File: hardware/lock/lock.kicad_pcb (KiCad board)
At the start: 2 copper layers, 64 x 23 mm, 50 parts, among them J2 I2C JST-PH RA, J3 SOLENOID 12V, J4 UPDI PROG, J5 SERVO S/V+/GND, J6 HALL DOOR, J7 HALL BOLT, J8 SERVO2 S/V+/GND, Q1 AO3400A, Q2 AO3400A, Q3 AO3401A, Q4 AO3400A, Q5 AO3400A, U1 ATtiny1616, U2 MT3608

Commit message: lock: PCB checkpoint — footprint placement progress
Co-Authored-By: Claude Opus 4.8 (1M context) <noreply@anthropic.com>
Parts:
- moved C6 4.05 mm to (133.9, 68.0), turned to -90 degrees
- moved C4 2.25 mm to (131.0, 68.0)
- moved Q3 0.24 mm to (129.2, 72.1)
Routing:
- net /DRV/VSERVO: track 26.3 -> 23.1 mm
- net Net-(U2-FB): track 16.8 -> 19.4 mm
- net SERVO_SIG: track 65.2 -> 63.0 mm
- net VCC: track 71.5 -> 70.0 mm, vias 12 -> 11
- net VSOL: track 37.4 -> 38.4 mm
- net GND: track 17.4 -> 18.4 mm, vias 58 -> 69
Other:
- board text added: "Ephemerkey LockBoost RevA"

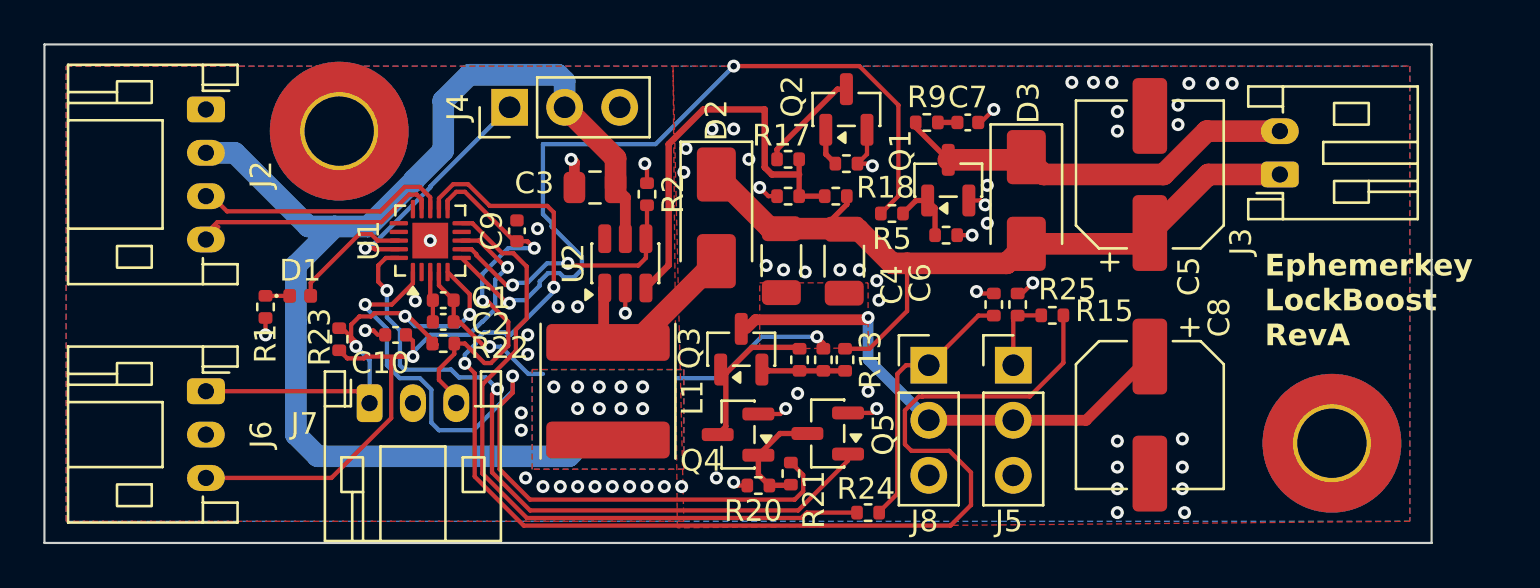
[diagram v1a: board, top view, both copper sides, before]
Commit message: lock: power from I2C connector (VSYS), LED on PC3; route board; ephemerkey J2=VSYS
Power move: the lock has NO local battery (J1 removed) — VCC and the boost/
actuator draw come from ephemerkey's VSYS rail over the I2C connector (J2.2).
- ephemerkey: J2.2 = VSYS (was +3V3); manifest note + DESIGN.md updated, regenerated.
- lock: README interface/architecture/BOM + servo source (R13=VSOL / R14=VSYS,
  no more VBAT) updated to match the as-wired board.
- Caveat documented: a 12V solenoid pull-in (~3-4A) exceeds a JST-PH contact and
  ephemerkey's load-share; favor the 6V servo / low-duty, or a dedicated feed.
- I2C pull-ups stay on ephemerkey at +3V3 (STM32 pins not >3.6V tolerant).

LED move: status LED (D1) is driven by PC3, not PA3 (PA3 now spare). Docs + manifest.

lock schematic + PCB are now hand-wired and fully routed (DRC: 0 unconnected,
0 schematic-parity). Manifest marked REFERENCE-OF-RECORD — do not regenerate
(would destroy the wiring). Verified with KiCad's own kicad-cli ERC/DRC.

Pending (owner fixing): PWR_FLAGs on VCC/GND, NC flags on unused pins, J6/J7 GND
thermal relief, minor stub/silk cleanups.

Co-Authored-By: Claude Opus 4.8 (1M context) <noreply@anthropic.com>
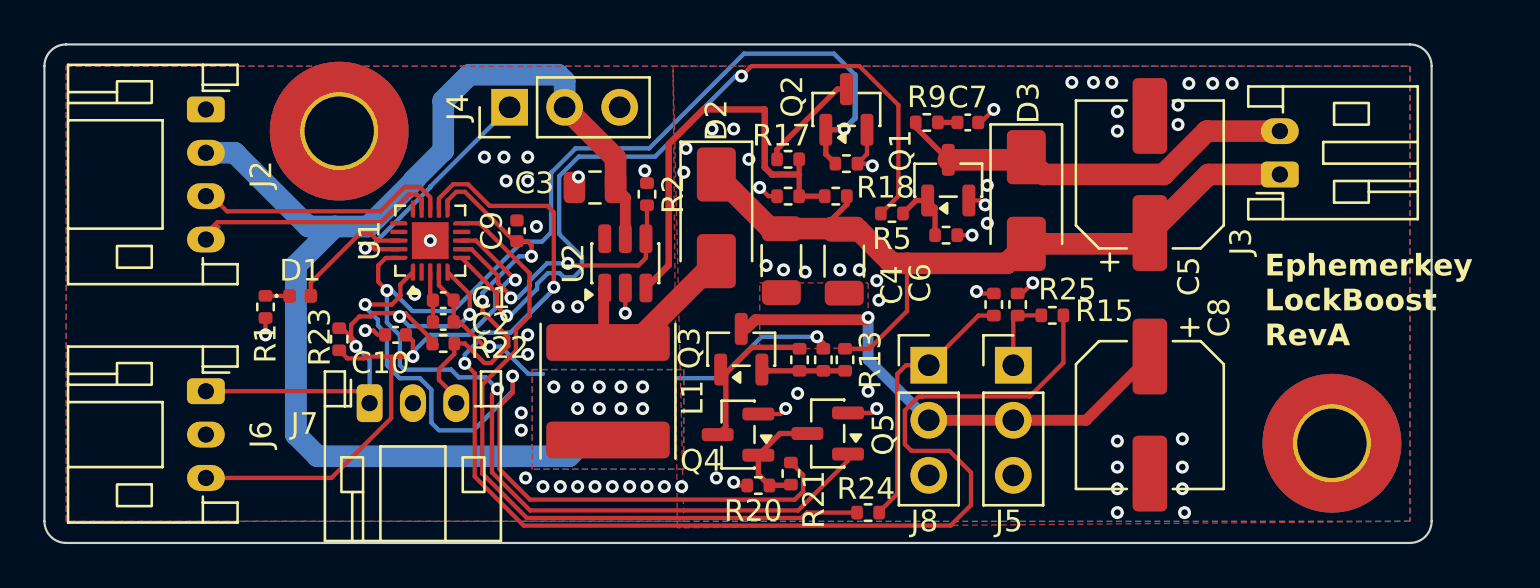
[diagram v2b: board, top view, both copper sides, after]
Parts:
- U1: footprint Package_DFN_QFN:QFN-20-1EP_3x3mm_P0.4mm_EP1.65x1.65mm -> Package_DFN_QFN:VQFN-20-1EP_3x3mm_P0.4mm_EP1.7x1.7mm
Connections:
- Q2 pad 1: BOOST_VEL -> BOOST_VSEL
- R18 pad 1: BOOST_VEL -> BOOST_VSEL
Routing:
- net BOOST_VSEL: track 33.6 -> 68.0 mm, vias 2 -> 3
- net BOOST_VEL: track 1.74 -> 0.00 mm
- net GND: track 18.4 -> 17.3 mm, vias 69 -> 74
- net SOL_PWM: track 37.8 -> 36.8 mm
- net SOL_BOOST_EN: track 12.3 -> 13.1 mm
- net /MCU/HALL_DOOR: track 27.6 -> 28.3 mm
- net /MCU/HALL_BOLT: track 19.3 -> 18.7 mm
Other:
- outline, holes or cut-outs redrawn

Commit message: lock: PCB edits — DRC/ERC cleanup in progress
Co-Authored-By: Claude Opus 4.8 (1M context) <noreply@anthropic.com>
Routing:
- net /MCU/HALL_DOOR: track 28.3 -> 27.8 mm
- net GND: vias 74 -> 75
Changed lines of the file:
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@@
+	)
+	(via
+		(at 130.75047 71.225)
+		(size 0.6)
+		(drill 0.3)
+		(layers "F.Cu" "B.Cu")
+		(free yes)
+		(net "GND")
 	)
 	(via
@@
 	)
 	(via
-		(at 131.1 68.4)
+		(at 131.2 68.2)
 		(size 0.6)
 		(drill 0.3)
@@
 	)
 	(via
-		(at 132.1 68.5)
+		(at 132.4 68.2)
 		(size 0.6)
 		(drill 0.3)
@@
 	)
 	(segment
-		(start 118.366486 68.507526)
-		(end 118.729265 68.870305)
-		(width 0.2)
-		(layer "F.Cu")
-		(net "/MCU/HALL_DOOR")
-	)
-	(segment
 		(start 110.97471 72.48471)
 		(end 111.741798 72.48471)
@@
 		(layer "B.Cu")
 		(net "/MCU/HALL_DOOR")
+	)
+	(segment
+		(start 129.3875 71.1125)
+		(end 130.05 70.45)
+		(width 0.5)
+		(layer "F.Cu")
+		(net "/DRV/VSERVO")
 	)
 	(segment
@@
 	)
 	(segment
+		(start 130.05 70.45)
+		(end 133.181371 70.45)
+		(width 0.5)
+		(layer "F.Cu")
+		(net "/DRV/VSERVO")
+	)
+	(segment
+		(start 133.181371 70.45)
+		(end 133.431371 70.7)
+		(width 0.5)
+		(layer "F.Cu")
+		(net "/DRV/VSERVO")
+	)
+	(segment
+		(start 145.06 75.34)
+		(end 141.7 75.34)
+		(width 0.5)
+		(layer "F.Cu")
+		(net "/DRV/VSERVO")
+	)
+	(segment
+		(start 141.7 75.34)
+		(end 137.8 75.34)
+		(width 0.5)
+		(layer "F.Cu")
+		(net "/DRV/VSERVO")
+	)
+	(segment
+		(start 133.431371 70.7)
+		(end 134.9 70.7)
+		(width 0.5)
+		(layer "F.Cu")
+		(net "/DRV/VSERVO")
+	)
+	(segment
 		(start 134.9 70.7)
 		(end 135 70.6)
@@
 		(net "/DRV/VSERVO")
 	)
-	(segment
-		(start 145.06 75.34)
-		(end 141.7 75.34)
-		(width 0.5)
-		(layer "F.Cu")
-		(net "/DRV/VSERVO")
-	)
-	(segment
-		(start 129.8 70.7)
-		(end 134.9 70.7)
-		(width 0.5)
-		(layer "F.Cu")
-		(net "/DRV/VSERVO")
-	)
-	(segment
-		(start 141.7 75.34)
-		(end 137.8 75.34)
-		(width 0.5)
-		(layer "F.Cu")
-		(net "/DRV/VSERVO")
-	)
-	(segment
-		(start 129.3875 71.1125)
-		(end 129.8 70.7)
-		(width 0.5)
-		(layer "F.Cu")
-		(net "/DRV/VSERVO")
-	)
 	(via
 		(at 135 70.6)
@@
 		(start 136.8 70.3)
 		(end 136.8 68.1)
-		(width 0.2)
+		(width 0.4)
 		(layer "F.Cu")
 		(net "VSOL")
@@
 		(start 135.06 72.04)
 		(end 136.8 70.3)
-		(width 0.2)
+		(width 0.4)
 		(layer "F.Cu")
 		(net "VSOL")
@@
 		(start 133.9375 72.04)
 		(end 135.06 72.04)
-		(width 0.2)
+		(width 0.4)
 		(layer "F.Cu")
 		(net "VSOL")
@@
 	)
 	(segment
-		(start 132.9375 71.770001)
-		(end 132.65534 71.487841)
-		(width 0.2)
+		(start 132.9375 72.04)
+		(end 132.9375 71.3375)
+		(width 0.4)
 		(layer "F.Cu")
 		(net "VCC")
@@
 		(start 115.2 69.12)
 		(end 115.88 69.8)
-		(width 0.2)
-		(layer "F.Cu")
-		(net "VCC")
-	)
-	(segment
-		(start 132.65534 71.487841)
-		(end 132.643531 71.487841)
 		(width 0.2)
 		(layer "F.Cu")
@@
 	)
 	(segment
-		(start 132.9375 72.04)
-		(end 132.9375 71.770001)
-		(width 0.2)
-		(layer "F.Cu")
-		(net "VCC")
-	)
-	(segment
 		(start 123.35 63.25)
 		(end 123.35 64.6)
@@
 		(net "VCC")
 	)
+	(segment
+		(start 132.9375 71.3375)
+		(end 132.8 71.2)
+		(width 0.2)
+		(layer "F.Cu")
+		(net "VCC")
+	)
 	(via
 		(at 122.6 73.8)
@@
 	)
 	(via
-		(at 132.643531 71.487841)
+		(at 132.8 71.2)
 		(size 0.6)
 		(drill 0.3)
@@
 	)
 	(segment
+		(start 130.419099 72.025)
+		(end 131.975 72.025)
+		(width 0.5)
+		(layer "B.Cu")
+		(net "VCC")
+	)
+	(segment
 		(start 118.063861 71.942175)
 		(end 117.542173 71.942175)
@@
 	)
 	(segment
+		(start 126.2 73.4)
+		(end 128.175516 73.4)
+		(width 0.5)
+		(layer "B.Cu")
+		(net "VCC")
+	)
+	(segment
 		(start 115.4 60.6)
 		(end 116.6 59.4)
@@
 	)
 	(segment
-		(start 128.175516 73.4)
-		(end 130.087675 71.487841)
-		(width 0.2)
-		(layer "B.Cu")
-		(net "VCC")
-	)
-	(segment
 		(start 109.175 66.4)
 		(end 110.4 66.4)
@@
 	)
 	(segment
-		(start 126.2 73.4)
-		(end 128.175516 73.4)
-		(width 0.2)
+		(start 131.975 72.025)
+		(end 132.8 71.2)
+		(width 0.5)
+		(layer "B.Cu")
+		(net "VCC")
+	)
+	(segment
+		(start 129.844099 72.6)
+		(end 130.419099 72.025)
+		(width 0.5)
 		(layer "B.Cu")
 		(net "VCC")
@@
 	)
 	(segment
-		(start 130.087675 71.487841)
-		(end 132.643531 71.487841)
-		(width 0.2)
-		(layer "B.Cu")
-		(net "VCC")
-	)
-	(segment
 		(start 119.321686 73.2)
 		(end 118.063861 71.942175)
@@
 	)
 	(segment
+		(start 128.175516 73.4)
+		(end 128.975516 72.6)
+		(width 0.5)
+		(layer "B.Cu")
+		(net "VCC")
+	)
+	(segment
+		(start 128.975516 72.6)
+		(end 129.844099 72.6)
+		(width 0.5)
+		(layer "B.Cu")
+		(net "VCC")
+	)
+	(segment
 		(start 131.7725 71.975)
 		(end 129.642696 71.975)
@@
 		(start 132.9375 73.06)
 		(end 131.8375 73.06)
-		(width 0.25)
+		(width 0.4)
 		(layer "F.Cu")
 		(net "/DRV/VSERVO_SRC")
@@
 		(start 133.9375 73.06)
 		(end 132.9375 73.06)
-		(width 0.25)
+		(width 0.4)
 		(layer "F.Cu")
 		(net "/DRV/VSERVO_SRC")
@@
 		(start 131.8375 73.06)
 		(end 130.41 73.06)
-		(width 0.25)
+		(width 0.4)
 		(layer "F.Cu")
 		(net "/DRV/VSERVO_SRC")
@@
 			(thermal_gap 0.5)
 			(thermal_bridge_width 0.5)
-			(smoothing chamfer)
+			(smoothing fillet)
+			(radius 1)
 			(island_removal_mode 0)
 		)
@@
 			(thermal_gap 0.5)
 			(thermal_bridge_width 0.5)
-			(smoothing chamfer)
+			(smoothing fillet)
+			(radius 1)
 			(island_removal_mode 0)
 		)
